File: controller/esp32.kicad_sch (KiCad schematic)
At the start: 12 parts, among them J2 Conn_01x06, U3 NRF24L01_Breakout, U4 ADS7828, U5 ESP32-WROOM-32U

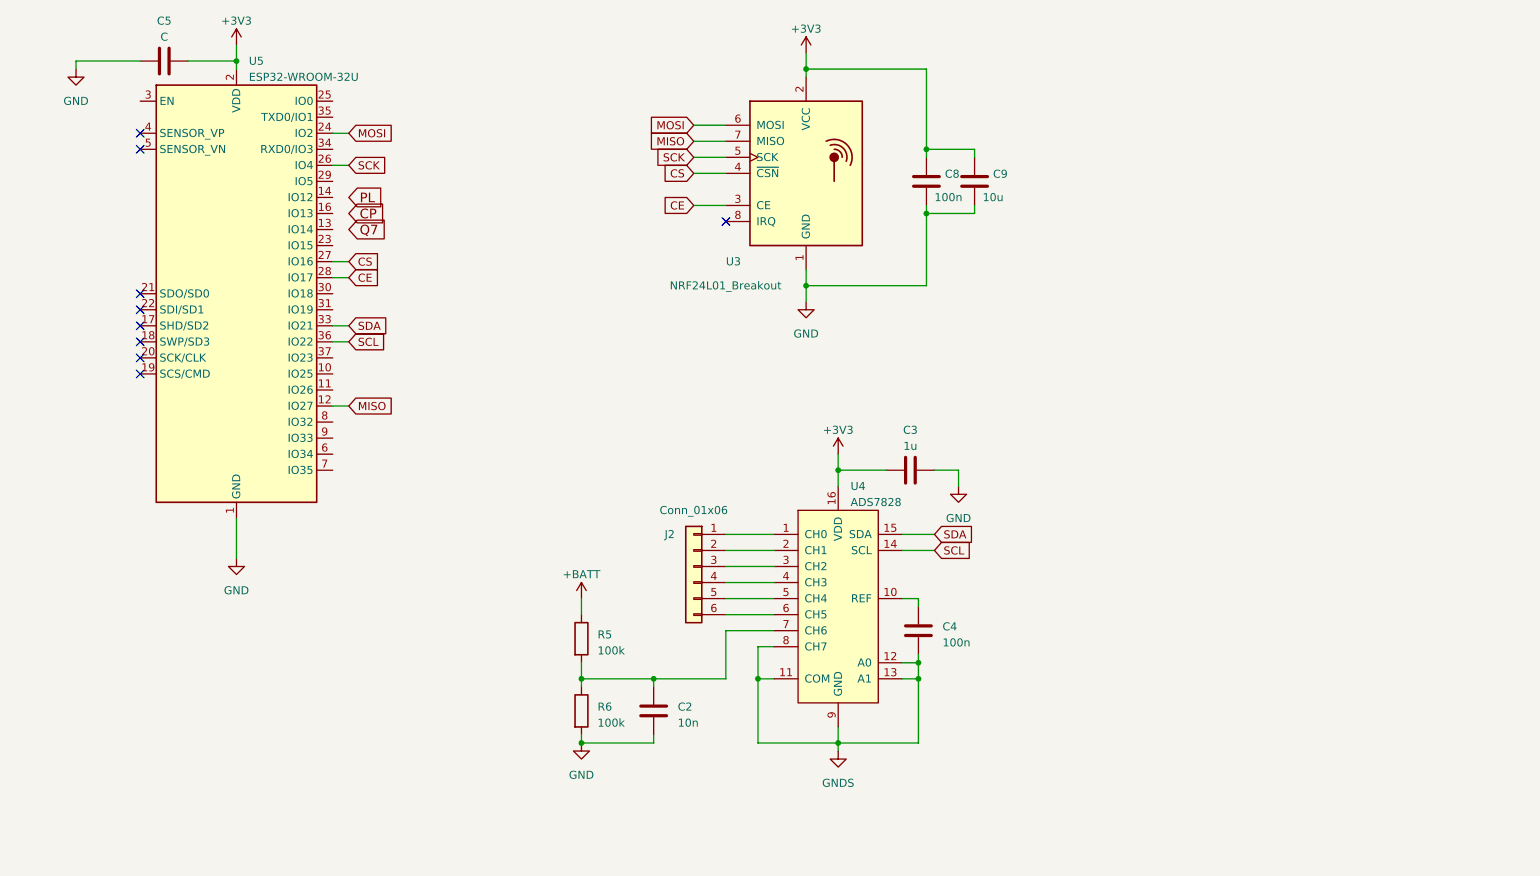
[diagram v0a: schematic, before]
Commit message: Add debug connector.
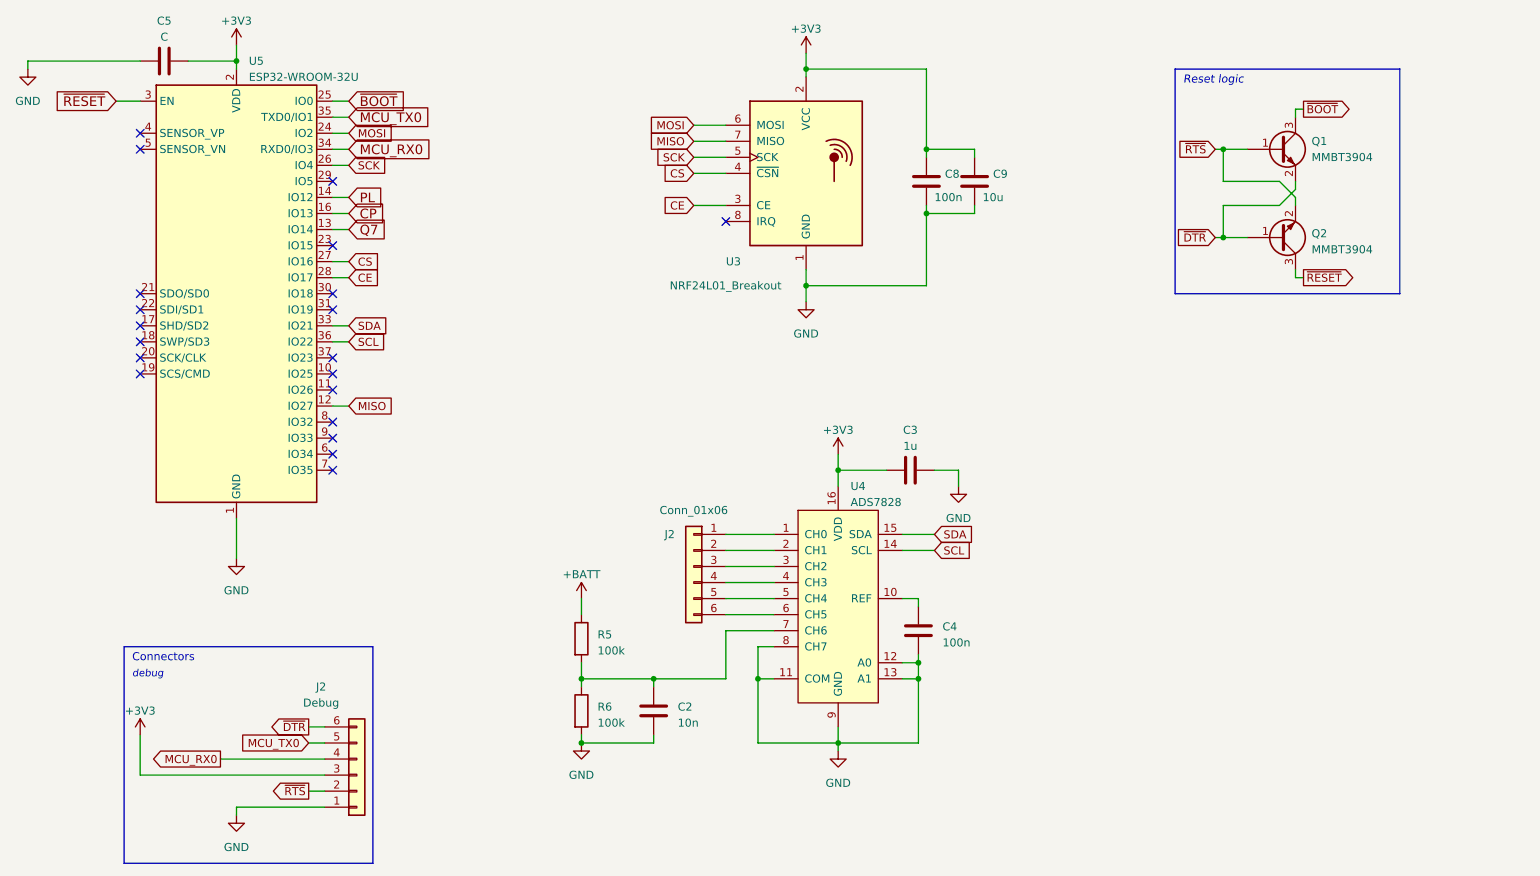
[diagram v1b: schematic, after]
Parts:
- added J2: Debug, Connector_PinHeader_2.54mm:PinHeader_1x06_P2.54mm_Vertical, symbol Connector_Generic:Conn_01x06
- added Q1, Q2: MMBT3904, Package_TO_SOT_SMD:SOT-23, symbol Transistor_BJT:MMBT3904
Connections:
- net GNDS is gone; now on net GND: C4.2, U4.11 (COM), U4.12 (A0), U4.13 (A1), U4.8 (CH7), U4.9 (GND)
- net +3V3: now also J2.3 (Pin_3)
- net CP: now also U5.16 (IO13)
- net GND: now also J2.1 (Pin_1)
- net PL: now also U5.14 (IO12)
- net Q7: now also U5.13 (IO14)
- net ~{BOOT}: now reaches U5.25 (IO0)
- net ~{BOOT}: now also Q1.3 (C)
- net ~{RESET}: now reaches U5.3 (EN)
- net ~{RESET}: now also Q2.3 (C)
- net MCU_RX0: now reaches U5.34 (RXD0/IO3)
- net MCU_RX0: now also J2.4 (Pin_4)
- net MCU_TX0: now reaches U5.35 (TXD0/IO1)
- net MCU_TX0: now also J2.5 (Pin_5)
- new net ~{DTR}: J2.6 (Pin_6), Q1.2 (E), Q2.1 (B)
- new net ~{RTS}: J2.2 (Pin_2), Q1.1 (B), Q2.2 (E)
- no-connect marks 9 -> 20
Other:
- note added: "Connectors"
- note added: "Reset logic"
- note added: "debug"

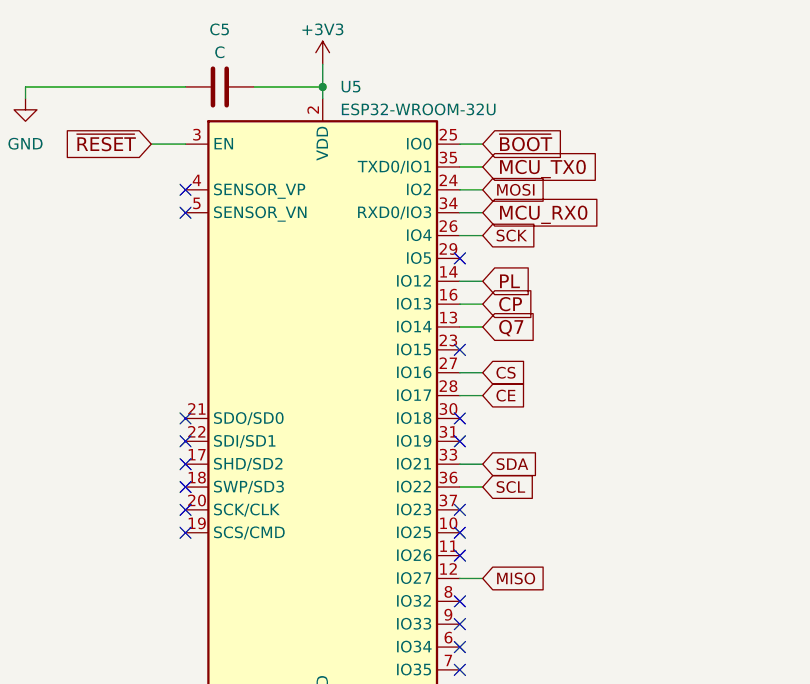
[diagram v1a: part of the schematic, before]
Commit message: Fix capacitor values.
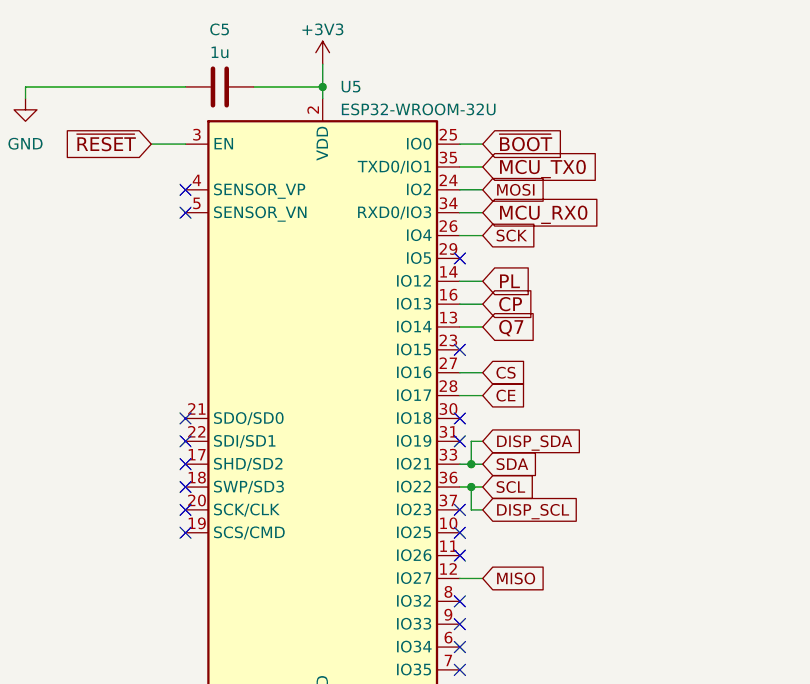
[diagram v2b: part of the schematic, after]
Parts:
- C5: value C -> 1u
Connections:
- net SCL renamed DISP_SCL
- net SDA renamed DISP_SDA
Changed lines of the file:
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@@
   (junction (at 156.21 45.72) (diameter 0) (color 0 0 0 0)
+  )
+  (junction (at 82.55 88.9) (diameter 0) (color 0 0 0 0)
+  )
+  (junction (at 82.55 86.36) (diameter 0) (color 0 0 0 0)
   )
   (junction (at 120.65 142.24) (diameter 0) (color 0 0 0 0)
@@
     (stroke (width 0) (type default))
   )
+  (wire (pts (xy 82.55 91.44) (xy 83.82 91.44))
+    (stroke (width 0) (type default))
+  )
   (wire (pts (xy 132.08 142.24) (xy 120.65 142.24))
     (stroke (width 0) (type default))
@@
     (stroke (width 0) (type default))
   )
+  (wire (pts (xy 82.55 88.9) (xy 82.55 91.44))
+    (stroke (width 0) (type default))
+  )
+  (wire (pts (xy 82.55 86.36) (xy 81.28 86.36))
+    (stroke (width 0) (type default))
+  )
+  (wire (pts (xy 82.55 88.9) (xy 83.82 88.9))
+    (stroke (width 0) (type default))
+  )
   (wire (pts (xy 161.29 106.68) (xy 161.29 109.22))
     (stroke (width 0) (type default))
@@
     (stroke (width 0) (type default))
   )
-  (wire (pts (xy 83.82 86.36) (xy 81.28 86.36))
+  (wire (pts (xy 83.82 86.36) (xy 82.55 86.36))
     (stroke (width 0) (type default))
   )
@@
     (stroke (width 0) (type default))
   )
+  (wire (pts (xy 82.55 83.82) (xy 82.55 86.36))
+    (stroke (width 0) (type default))
+  )
   (wire (pts (xy 175.26 68.58) (xy 182.88 68.58))
     (stroke (width 0) (type default))
@@
     (stroke (width 0) (type default))
   )
-  (wire (pts (xy 81.28 88.9) (xy 83.82 88.9))
+  (wire (pts (xy 83.82 83.82) (xy 82.55 83.82))
+    (stroke (width 0) (type default))
+  )
+  (wire (pts (xy 81.28 88.9) (xy 82.55 88.9))
     (stroke (width 0) (type default))
   )
@@
     )
   )
+  (global_label "DISP_SDA" (shape input) (at 83.82 83.82 0) (fields_autoplaced)
+    (effects (font (size 1.27 1.27)) (justify left))
+    (property "Intersheetrefs" "${INTERSHEET_REFS}" (at 94.9616 83.82 0)
+      (effects (font (size 1.27 1.27)) (justify left) hide)
+    )
+  )
   (global_label "MCU_RX0" (shape output) (at 63.5 154.94 180) (fields_autoplaced)
     (effects (font (size 1.27 1.27)) (justify right))
     (property "Intersheetrefs" "${INTERSHEET_REFS}" (at 51.8857 154.94 0)
       (effects (font (size 1.27 1.27)) (justify right) hide)
+    )
+  )
+  (global_label "DISP_SCL" (shape input) (at 83.82 91.44 0) (fields_autoplaced)
+    (effects (font (size 1.27 1.27)) (justify left))
+    (property "Intersheetrefs" "${INTERSHEET_REFS}" (at 94.9011 91.44 0)
+      (effects (font (size 1.27 1.27)) (justify left) hide)
     )
   )
@@
       (effects (font (size 1.27 1.27)))
     )
-    (property "Value" "C" (at 54.61 40.64 90)
+    (property "Value" "1u" (at 54.61 40.64 90)
       (effects (font (size 1.27 1.27)))
     )

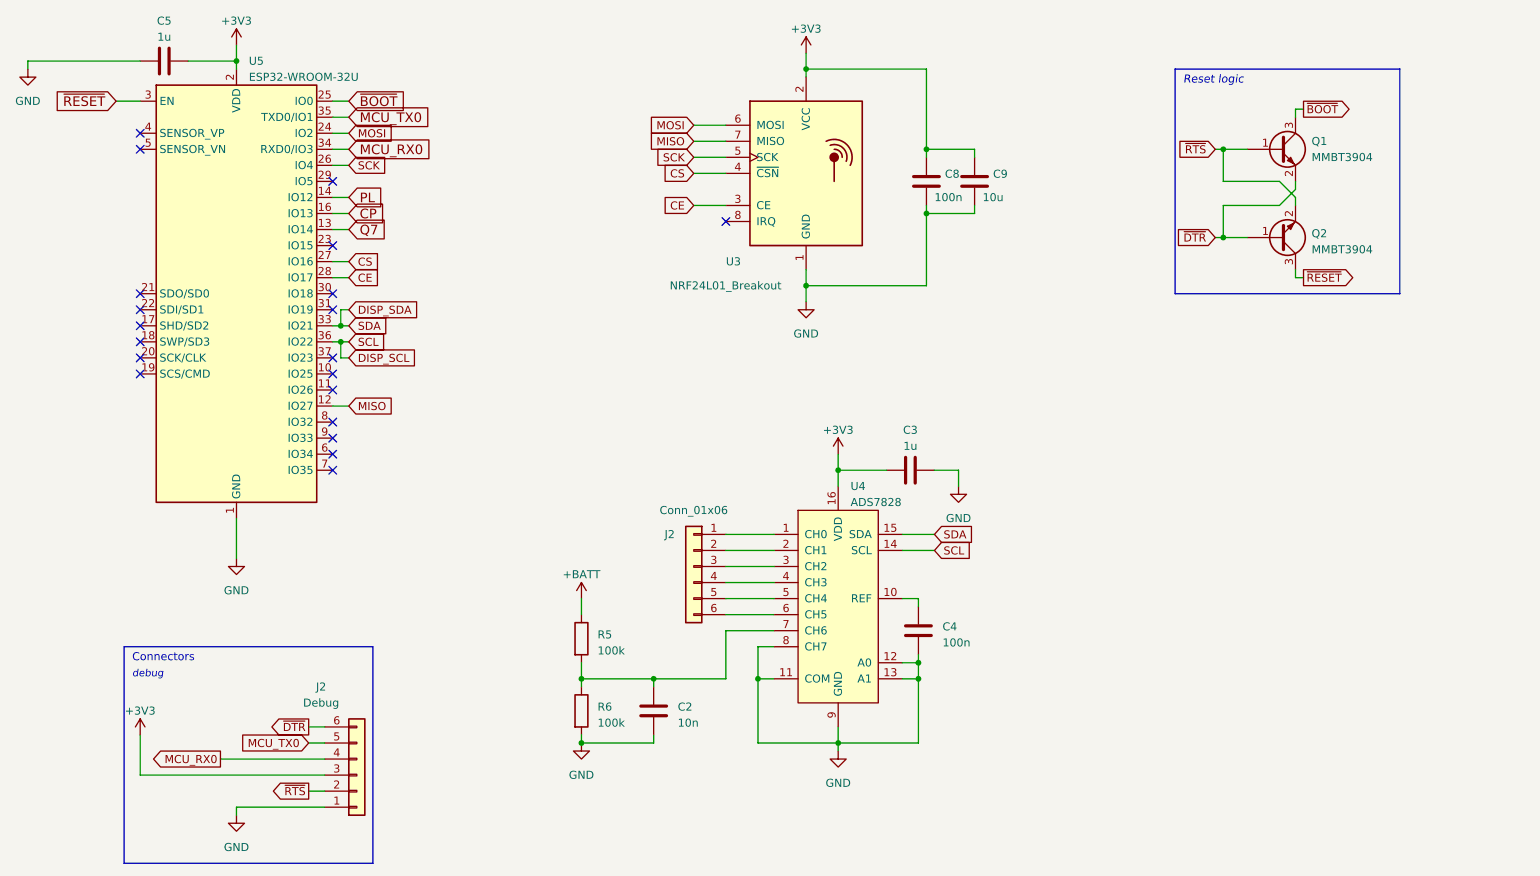
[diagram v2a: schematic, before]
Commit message: Add switches, regulator, etc.
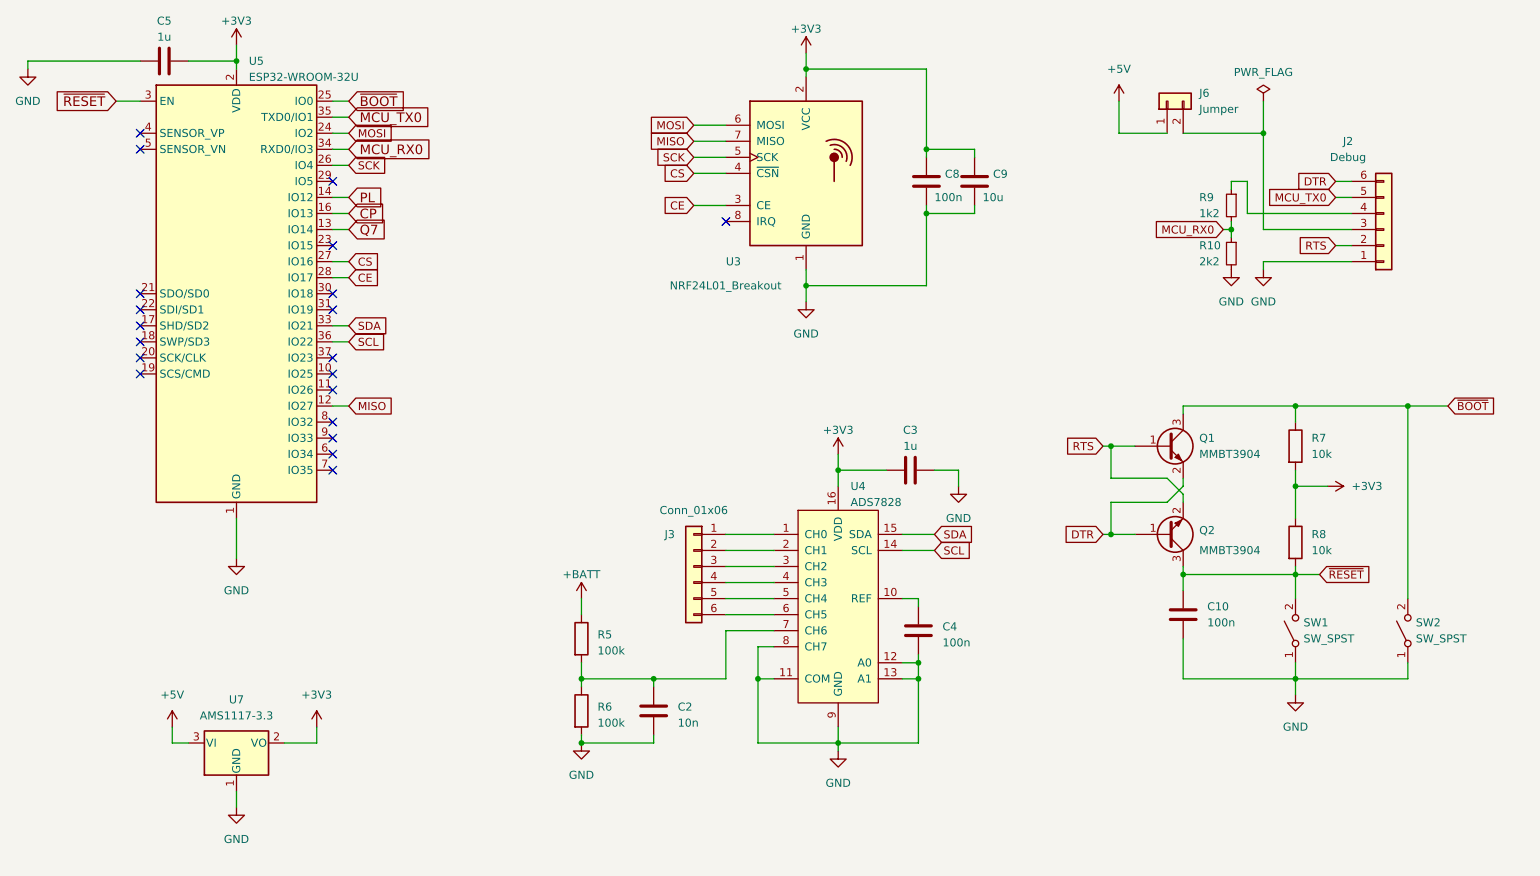
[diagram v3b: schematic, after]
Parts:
- added C10: 100n, Capacitor_SMD:C_0603_1608Metric, symbol Device:C
- added J6: Jumper, Connector_PinHeader_2.54mm:PinHeader_1x02_P2.54mm_Vertical, symbol Connector_Generic:Conn_01x02
- added R10: 2k2, Resistor_SMD:R_0603_1608Metric, symbol Device:R_Small
- added R7, R8: 10k, Resistor_SMD:R_0603_1608Metric, symbol Device:R
- added R9: 1k2, Resistor_SMD:R_0603_1608Metric, symbol Device:R_Small
- added SW1, SW2: SW_SPST, Button_Switch_SMD:SW_SPST_CK_RS282G05A3, symbol switches:SW_SPST
- added U7: AMS1117-3.3, Package_TO_SOT_SMD:SOT-223-3_TabPin2, symbol Regulator_Linear:AMS1117-3.3
- renumbered J2 to J3
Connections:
- net +3V3: now also R7.2, R8.1, U7.2 (VO); no longer J2.3 (Pin_3)
- net GND: now also C10.2, R10.2, SW1.1 (A), SW2.1 (A), U7.1 (GND)
- net MCU_RX0: now also R10.1, R9.2; no longer J2.4 (Pin_4)
- net ~{BOOT}: now also R7.1, SW2.2 (B)
- net ~{RESET}: now also C10.1, R8.2, SW1.2 (B)
- net DISP_SCL renamed SCL
- net DISP_SDA renamed SDA
- net ~{DTR} renamed DTR
- net ~{RTS} renamed RTS
- new net: J2.3 (Pin_3), J6.2 (Pin_2)
- new net: J2.4 (Pin_4), R9.1
- new net +5V: J6.1 (Pin_1), U7.3 (VI)
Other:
- note removed: "Connectors"
- note removed: "Reset logic"
- note removed: "debug"
